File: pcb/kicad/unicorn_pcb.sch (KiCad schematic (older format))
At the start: 26 parts, among them J1 Conn_01x10_Male_LEFT, J2 Conn_01x10_Male_RIGHT, SW1 SW_Push

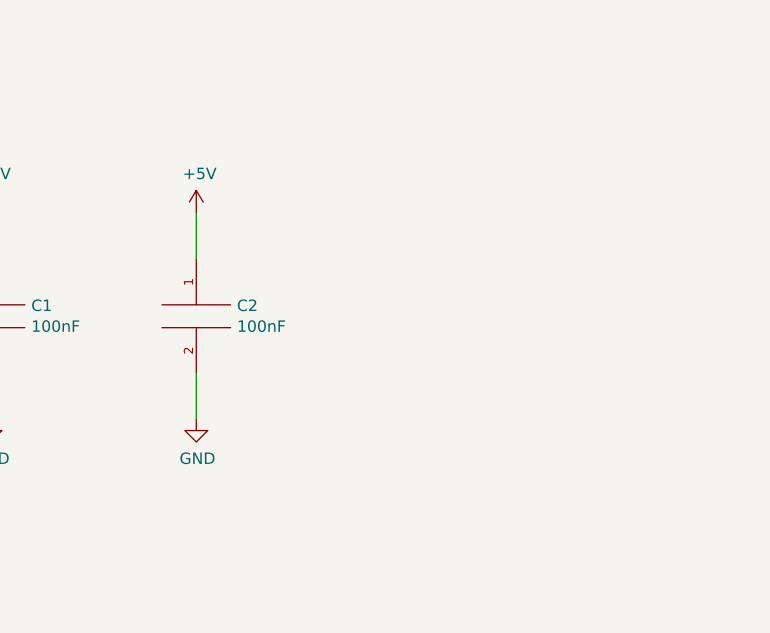
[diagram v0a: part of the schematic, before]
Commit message: pcb rev 1.1; extended board test firmware
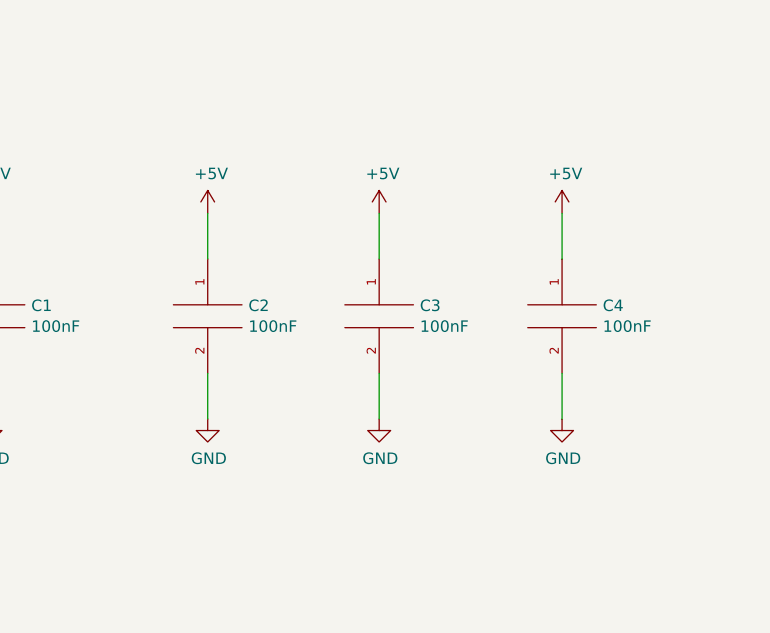
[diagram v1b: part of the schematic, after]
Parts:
- added C3, C4: 100nF, Capacitor_SMD:C_1206_3216Metric_Pad1.42x1.75mm_HandSolder, symbol pspice:C
- J2: footprint Connector_PinHeader_2.54mm:PinHeader_1x10_P2.54mm_Vertical_SMD_Pin1Left -> Connector_PinHeader_2.54mm:PinHeader_1x10_P2.54mm_Vertical_SMD_Pin1Right
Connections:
- net +5V: now also C3.1, C4.1
- net GND: now also C3.2, C4.2
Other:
- moved on the sheet: C2
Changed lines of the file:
@@
 F 0 "J2" H 2406 6178 50  0000 C CNN
 F 1 "Conn_01x10_Male_RIGHT" H 2406 6087 50  0000 C CNN
-F 2 "Connector_PinHeader_2.54mm:PinHeader_1x10_P2.54mm_Vertical_SMD_Pin1Left" H 2300 5600 50  0001 C CNN
+F 2 "Connector_PinHeader_2.54mm:PinHeader_1x10_P2.54mm_Vertical_SMD_Pin1Right" H 2300 5600 50  0001 C CNN
 F 3 "~" H 2300 5600 50  0001 C CNN
 	1    2300 5600
@@
 L pspice:C C2
 U 1 1 5C70E4D8
-P 8700 5450
-F 0 "C2" H 8878 5496 50  0000 L CNN
-F 1 "100nF" H 8878 5405 50  0000 L CNN
-F 2 "Capacitor_SMD:C_1206_3216Metric_Pad1.42x1.75mm_HandSolder" H 8700 5450 50  0001 C CNN
-F 3 "~" H 8700 5450 50  0001 C CNN
-	1    8700 5450
+P 8750 5450
+F 0 "C2" H 8928 5496 50  0000 L CNN
+F 1 "100nF" H 8928 5405 50  0000 L CNN
+F 2 "Capacitor_SMD:C_1206_3216Metric_Pad1.42x1.75mm_HandSolder" H 8750 5450 50  0001 C CNN
+F 3 "~" H 8750 5450 50  0001 C CNN
+	1    8750 5450
 	1    0    0    -1
 $EndComp
@@
 L power:GND #PWR0104
 U 1 1 5C70EEA0
-P 8700 5900
-F 0 "#PWR0104" H 8700 5650 50  0001 C CNN
-F 1 "GND" H 8705 5727 50  0000 C CNN
-F 2 "" H 8700 5900 50  0001 C CNN
-F 3 "" H 8700 5900 50  0001 C CNN
-	1    8700 5900
+P 8750 5900
+F 0 "#PWR0104" H 8750 5650 50  0001 C CNN
+F 1 "GND" H 8755 5727 50  0000 C CNN
+F 2 "" H 8750 5900 50  0001 C CNN
+F 3 "" H 8750 5900 50  0001 C CNN
+	1    8750 5900
 	1    0    0    -1
 $EndComp
@@
 L power:+5V #PWR0106
 U 1 1 5C70F3F3
-P 8700 5000
-F 0 "#PWR0106" H 8700 4850 50  0001 C CNN
-F 1 "+5V" H 8715 5173 50  0000 C CNN
-F 2 "" H 8700 5000 50  0001 C CNN
-F 3 "" H 8700 5000 50  0001 C CNN
-	1    8700 5000
-	1    0    0    -1
-$EndComp
-Wire Wire Line
-	8700 5000 8700 5200
-Wire Wire Line
-	8700 5700 8700 5900
+P 8750 5000
+F 0 "#PWR0106" H 8750 4850 50  0001 C CNN
+F 1 "+5V" H 8765 5173 50  0000 C CNN
+F 2 "" H 8750 5000 50  0001 C CNN
+F 3 "" H 8750 5000 50  0001 C CNN
+	1    8750 5000
+	1    0    0    -1
+$EndComp
+Wire Wire Line
+	8750 5000 8750 5200
+Wire Wire Line
+	8750 5700 8750 5900
 Wire Wire Line
 	7800 5000 7800 5200
@@
 Text Notes 10650 7600 0    50   ~ 0
 1
+$Comp
+L pspice:C C3
+U 1 1 5CBD0116
+P 9500 5450
+F 0 "C3" H 9678 5496 50  0000 L CNN
+F 1 "100nF" H 9678 5405 50  0000 L CNN
+F 2 "Capacitor_SMD:C_1206_3216Metric_Pad1.42x1.75mm_HandSolder" H 9500 5450 50  0001 C CNN
+F 3 "~" H 9500 5450 50  0001 C CNN
+	1    9500 5450
+	1    0    0    -1
+$EndComp
+$Comp
+L power:GND #PWR0107
+U 1 1 5CBD011D
+P 9500 5900
+F 0 "#PWR0107" H 9500 5650 50  0001 C CNN
+F 1 "GND" H 9505 5727 50  0000 C CNN
+F 2 "" H 9500 5900 50  0001 C CNN
+F 3 "" H 9500 5900 50  0001 C CNN
+	1    9500 5900
+	1    0    0    -1
+$EndComp
+$Comp
+L power:+5V #PWR0108
+U 1 1 5CBD0123
+P 9500 5000
+F 0 "#PWR0108" H 9500 4850 50  0001 C CNN
+F 1 "+5V" H 9515 5173 50  0000 C CNN
+F 2 "" H 9500 5000 50  0001 C CNN
+F 3 "" H 9500 5000 50  0001 C CNN
+	1    9500 5000
+	1    0    0    -1
+$EndComp
+Wire Wire Line
+	9500 5000 9500 5200
+Wire Wire Line
+	9500 5700 9500 5900
+$Comp
+L pspice:C C4
+U 1 1 5CBD2556
+P 10300 5450
+F 0 "C4" H 10478 5496 50  0000 L CNN
+F 1 "100nF" H 10478 5405 50  0000 L CNN
+F 2 "Capacitor_SMD:C_1206_3216Metric_Pad1.42x1.75mm_HandSolder" H 10300 5450 50  0001 C CNN
+F 3 "~" H 10300 5450 50  0001 C CNN
+	1    10300 5450
+	1    0    0    -1
+$EndComp
+$Comp
+L power:GND #PWR0109
+U 1 1 5CBD255D
+P 10300 5900
+F 0 "#PWR0109" H 10300 5650 50  0001 C CNN
+F 1 "GND" H 10305 5727 50  0000 C CNN
+F 2 "" H 10300 5900 50  0001 C CNN
+F 3 "" H 10300 5900 50  0001 C CNN
+	1    10300 5900
+	1    0    0    -1
+$EndComp
+$Comp
+L power:+5V #PWR0110
+U 1 1 5CBD2563
+P 10300 5000
+F 0 "#PWR0110" H 10300 4850 50  0001 C CNN
+F 1 "+5V" H 10315 5173 50  0000 C CNN
+F 2 "" H 10300 5000 50  0001 C CNN
+F 3 "" H 10300 5000 50  0001 C CNN
+	1    10300 5000
+	1    0    0    -1
+$EndComp
+Wire Wire Line
+	10300 5000 10300 5200
+Wire Wire Line
+	10300 5700 10300 5900
 $EndSCHEMATC
